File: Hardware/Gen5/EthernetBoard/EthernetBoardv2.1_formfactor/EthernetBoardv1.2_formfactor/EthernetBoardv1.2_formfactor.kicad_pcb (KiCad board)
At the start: 4 copper layers, 50 x 40 mm, 78 parts, among them J1 RJ45_Wuerth_7499010211A, J2 Conn_01x19_Pin, J3 Conn_01x19_Pin, J4 Conn_02x07_Odd_Even, J5 USB_C_Receptacle_USB2.0_16P, J6 Conn_01x02_Pin, J7 Conn_01x02_Pin, J9 Conn_01x02_Pin, Q1 SS8050, Q2 SS8050, SW1 SW_Push, SW2 SW_Push, U1 LAN8720A, U3 AMS1117-3.3, U4 CP2102N-Axx-xQFN28, U5 ESP32-WROVER-E-N8R8, Y1 ASCO

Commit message: updates
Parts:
- C14, C15, R13, R35: moved to B.Cu
- moved J2 94.4 mm to (241.2, 70.6)
- moved J3 90.7 mm to (241.2, 106.0)
- moved R13 47.2 mm to (206.7, 92.2), turned to 90 degrees
- moved R35 43.2 mm to (205.2, 96.0)
- moved R33 41.9 mm to (205.6, 96.1)
- moved R34 41.8 mm to (203.6, 95.9)
- moved Q1 41.4 mm to (208.7, 79.4)
- moved R17 40.7 mm to (213.0, 91.0)
- moved U4 40.5 mm to (206.2, 90.9)
- moved Q2 40.1 mm to (204.4, 85.6)
- moved C14 39.9 mm to (203.7, 92.2)
- moved C15 39.9 mm to (205.0, 92.2)
- moved SW2 39.8 mm to (212.8, 80.5), turned to -90 degrees
- moved D5 39.3 mm to (201.6, 95.7)
- moved R16 39.3 mm to (213.0, 88.3)
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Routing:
- net /EN: track 131.3 -> 77.5 mm, vias 1 -> 0
- net VBUS: track 44.9 -> 16.2 mm
- net /TXDUSB: track 58.6 -> 33.5 mm, vias 2 -> 1
- net /RXDUSB: track 54.0 -> 32.3 mm, vias 2 -> 1
- net /IO0: track 157.8 -> 137.7 mm, vias 3 -> 2
- net /TXD: track 19.3 -> 0.00 mm
- net GND: track 64.6 -> 46.4 mm, vias 31 -> 22
- net /DTR: track 16.5 -> 0.00 mm
- net /USB_DN: track 17.5 -> 1.70 mm
- net /RTS: track 13.8 -> 0.00 mm, vias 2 -> 0
- net /RXD: track 10.1 -> 0.00 mm
- net Net-(U4-VBUS): track 7.75 -> 0.00 mm
- net /USB_DP: track 9.20 -> 1.70 mm
- net Net-(U4-~{SUSPEND}): track 5.91 -> 0.00 mm
- net Net-(Q1-B): track 5.31 -> 0.00 mm
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
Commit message: update
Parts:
- removed J2, J3: Conn_01x19_Pin, Connector_PinHeader_2.54mm:PinHeader_1x19_P2.54mm_Vertical
- removed J4: Conn_02x07_Odd_Even, Connector_PinHeader_2.54mm:PinHeader_2x07_P2.54mm_Vertical
- removed J6, J7, J9: Conn_01x02_Pin, Connector_PinHeader_2.54mm:PinHeader_1x02_P2.54mm_Vertical
- removed TP1, TP2: TestPoint, TestPoint:TestPoint_Pad_2.0x2.0mm
- added R36: 10K, Resistor_SMD:R_0402_1005Metric, B.Cu at (208.3, 89.1)
- added R37: 0R, Resistor_SMD:R_0201_0603Metric, B.Cu at (191.4, 99.3)
- added R38: 0R, Resistor_SMD:R_0201_0603Metric, B.Cu at (198.0, 87.4)
- added R39: 0R, Resistor_SMD:R_0201_0603Metric, B.Cu at (177.8, 93.3)
- C1, C10, C11, C12, C13, C2, C5, C6, C7, C8, C9, D1, D2, D3, D5, D7, D8, L1, Q1, Q2, R1, R10, R11, R14, R15, R18, R19, R2, R20, R21, R22, R23, R3, R34, R4, R5, R6, R7, R8, R9, SW1, SW2, U1, U3, Y1: moved to B.Cu
- R12: footprint Jumper:SolderJumper-2_P1.3mm_Bridged2Bar_RoundedPad1.0x1.5mm -> Resistor_SMD:R_0201_0603Metric
- R16, R17, R24, R25, R26, R27, R28, R29, R30, R31, R32: footprint Jumper:SolderJumper-2_P1.3mm_Bridged2Bar_RoundedPad1.0x1.5mm -> Resistor_SMD:R_0201_0603Metric; moved to B.Cu
- moved R27 142.5 mm to (209.0, 100.8), turned to 90 degrees
- moved R28 138.0 mm to (205.2, 100.8), turned to 90 degrees
- moved R31 128.6 mm to (210.3, 100.8), turned to 90 degrees
- moved R30 123.2 mm to (201.4, 100.8), turned to 90 degrees
- moved R32 121.1 mm to (195.0, 103.1), turned to 90 degrees
- moved L1 120.5 mm to (191.8, 97.2), turned to -90 degrees
- moved R12 120.3 mm to (186.1, 97.2), turned to 0 degrees
- moved C8 117.5 mm to (194.5, 98.7)
- moved C4 117.4 mm to (207.1, 107.8), turned to -90 degrees
- moved R10 117.1 mm to (191.3, 92.6)
- moved R20 116.9 mm to (194.6, 97.3), turned to 180 degrees
- moved C11 116.8 mm to (190.9, 90.0), turned to 90 degrees
- moved C3 116.6 mm to (203.1, 107.4), turned to -90 degrees
- moved R8 116.3 mm to (190.3, 96.4), turned to 90 degrees
- moved U3 116.1 mm to (203.9, 107.7), turned to 0 degrees
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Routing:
- net /IO0: track 137.7 -> 0.00 mm, vias 2 -> 0
- net /TXD0: track 136.6 -> 0.00 mm, vias 1 -> 0
- net /RXD0: track 130.4 -> 0.00 mm, vias 3 -> 0
- net /IO21: track 122.9 -> 0.00 mm
- net VCC: track 117.3 -> 0.00 mm, vias 5 -> 0
- net /IO22: track 113.7 -> 0.00 mm, vias 2 -> 0
- net /IO18: track 88.8 -> 0.00 mm, vias 2 -> 0
- net /RXD1: track 85.4 -> 0.00 mm, vias 2 -> 0
- net /IO23: track 84.0 -> 0.00 mm
- net /EN: track 77.5 -> 0.00 mm
- net /CRS_DV: track 72.8 -> 0.00 mm, vias 2 -> 0
- net VDDA: track 70.0 -> 0.00 mm, vias 1 -> 0
- net +5V: track 63.5 -> 0.00 mm
- net GND: track 46.4 -> 0.00 mm, vias 22 -> 0
- net Net-(J1-Pad11): track 38.6 -> 0.00 mm
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- removed copper zone on B.Cu, net Earth
- removed copper zone on F.Cu, net Earth
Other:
- board size 50 x 40 mm -> 48 x 30 mm
- board text removed: "BOOT"
- board text removed: "EN"
- board text removed: "ESP32"
- board text removed: "Ethernet"
- board text removed: "Power"
- board text removed: "USB"

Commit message: updates
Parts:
- C7: footprint Capacitor_SMD:C_0603_1608Metric -> Capacitor_SMD:C_0402_1005Metric
- D8, R18, R39: moved to F.Cu
- moved D8 39.9 mm to (206.3, 109.6)
- moved R18 39.7 mm to (206.3, 106.5)
- moved D2 29.5 mm to (198.9, 108.1)
- moved R39 8.38 mm to (186.1, 92.0), turned to 0 degrees
- moved C1 7.12 mm to (193.8, 103.2), turned to 0 degrees
- moved SW1 2.85 mm to (193.8, 107.5), turned to -90 degrees
- moved U3 2.64 mm to (206.5, 108.2)
- moved C4 2.63 mm to (209.7, 108.2)
- moved R32 1.00 mm to (196.0, 103.1)
- moved C7 0.59 mm to (198.9, 95.0)
- moved C3 0.38 mm to (203.3, 107.1)
- moved R8 0.33 mm to (190.3, 96.7)
- moved R9 0.33 mm to (190.3, 94.7)
- moved R10 0.28 mm to (191.3, 92.3)
- moved D6 0.23 mm to (175.6, 105.9)
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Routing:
- net /EN: track 0.00 -> 54.1 mm, vias 0 -> 1
- net VBUS: track 0.00 -> 46.8 mm, vias 0 -> 1
- net GND: track 0.00 -> 39.5 mm, vias 0 -> 20
- net Net-(J1-Pad11): track 0.00 -> 37.8 mm
- net /RXD: track 0.00 -> 30.9 mm, vias 0 -> 1
- net /TXD: track 0.00 -> 30.3 mm, vias 0 -> 1
- net VDDA: track 0.00 -> 28.9 mm, vias 0 -> 1
- net /TD_N: track 0.00 -> 28.7 mm, vias 0 -> 1
- net /TD_P: track 0.00 -> 27.8 mm, vias 0 -> 1
- net Net-(J1-Pad10): track 0.00 -> 26.0 mm
- net Net-(J1-Pad8): track 0.00 -> 25.5 mm
- net +3.3V: track 0.00 -> 24.2 mm, vias 0 -> 15
- net /TXD1: track 0.00 -> 21.7 mm, vias 0 -> 2
- net /CRS_DV: track 0.00 -> 20.4 mm, vias 0 -> 2
- net /MDC: track 0.00 -> 18.4 mm, vias 0 -> 2
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- added copper zone on In2.Cu, net +3.3V
- added copper zone on B.Cu, net GND
- added copper zone on F.Cu, net GND
- added copper zone on In1.Cu, net GND

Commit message: done
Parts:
- moved C8 2.16 mm to (193.1, 100.3), turned to -90 degrees
- moved R22 2.11 mm to (195.1, 99.3), turned to 180 degrees
- moved R37 1.89 mm to (191.8, 101.1), turned to -90 degrees
- moved R20 0.60 mm to (195.1, 97.6), turned to -90 degrees
- moved R19 0.30 mm to (199.4, 100.1)
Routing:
- net VDDA: track 28.9 -> 62.8 mm, vias 1 -> 0
- net VCC: track 12.9 -> 34.2 mm, vias 2 -> 6
- net /TX_EN: track 0.00 -> 18.8 mm, vias 0 -> 2
- net /TXD0: track 1.69 -> 18.8 mm, vias 1 -> 2
- net GND: track 39.5 -> 53.1 mm, vias 20 -> 26
- net /CLK50: track 12.8 -> 20.6 mm
- net +3.3V: track 24.2 -> 27.8 mm
- net /REFCLKO: track 6.39 -> 3.53 mm
- net Net-(U4-VBUS): track 1.81 -> 4.31 mm, vias 0 -> 1
- net /nRST: track 2.99 -> 5.00 mm
- net +5V: track 7.53 -> 9.36 mm
- net /R_RX_CLK: track 3.34 -> 4.87 mm
- net /RXD: track 30.9 -> 31.7 mm

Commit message: stuff
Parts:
- added R40: 5.1k, Resistor_SMD:R_0603_1608Metric, B.Cu at (169.0, 108.1)
- added R41: 5.1k, Resistor_SMD:R_0603_1608Metric, B.Cu at (169.0, 106.3)
- added R42: 10K, Resistor_SMD:R_0402_1005Metric, F.Cu at (194.2, 105.5)
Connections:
- J5 pad A5: unconnected-(J5-CC1-PadA5) -> Net-(J5-CC1)
- J5 pad B5: unconnected-(J5-CC2-PadB5) -> Net-(J5-CC2)
- R19 pad 1: Net-(U1-MDIO) -> /MDIO
- U1 pad 12: Net-(U1-MDIO) -> /MDIO
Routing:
- net Net-(J5-CC1): track 0.00 -> 20.1 mm, vias 0 -> 1
- net /MDIO: track 0.00 -> 8.16 mm
- net Net-(U1-MDIO): track 5.38 -> 0.00 mm
- net Net-(J5-CC2): track 0.00 -> 4.18 mm
- net GND: track 53.1 -> 55.5 mm, vias 26 -> 28
- net /IO0: track 16.2 -> 17.4 mm
- net +3.3V: track 27.8 -> 28.8 mm, vias 15 -> 16

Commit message: stuff
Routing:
- net /IO0: vias 2 -> 1
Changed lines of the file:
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@@
 		(tags "resistor")
 		(property "Reference" "R22"
-			(at 0.1 0.9 0)
+			(at -0.91 1.3 90)
 			(layer "B.SilkS")
 			(effects
@@
 		(tags "capacitor")
 		(property "Reference" "C7"
-			(at 0 1.16 90)
+			(at 1.42 0 180)
 			(layer "B.SilkS")
 			(effects
 				(font
-					(size 1 1)
-					(thickness 0.15)
+					(size 0.5 0.5)
+					(thickness 0.125)
+					(bold yes)
 				)
 				(justify mirror)
@@
 		(tags "inductor")
 		(property "Reference" "L1"
-			(at 0.1 1.2 90)
+			(at 1.925 0.1 180)
 			(layer "B.SilkS")
 			(effects
@@
 		(tags "resistor")
 		(property "Reference" "R13"
-			(at 2 0 0)
+			(at 0.275 1.2 90)
 			(layer "B.SilkS")
 			(effects
@@
 		(tags "SOT TO_SOT_SMD")
 		(property "Reference" "Q1"
-			(at -1.3375 2.55 90)
+			(at -2.4375 0.95 180)
 			(layer "B.SilkS")
 			(effects
@@
 		(tags "resistor")
 		(property "Reference" "R7"
-			(at -1.49 0 0)
+			(at 0.025 0.9 90)
 			(layer "B.SilkS")
 			(effects
@@
 		(tags "resistor")
 		(property "Reference" "R20"
-			(at -1.81 0 90)
+			(at 0 0.9 90)
 			(layer "B.SilkS")
 			(effects
@@
 		(net 21)
 	)
-	(via
-		(at 194.8 104.4)
-		(size 0.6)
-		(drill 0.3)
-		(layers "F.Cu" "B.Cu")
-		(net 21)
-	)

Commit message: stuff
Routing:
- net GND: track 55.5 -> 54.8 mm, vias 28 -> 29
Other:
- board text added: "Ethernet Form Factor Gen 5 rev1.2"
- board text removed: "Ethernet Dev Board - Vine Internal rev 1.1 Charm Lab, Stanford October 19 2025"
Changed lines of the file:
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@@
 		(layer "Edge.Cuts")
 	)
-	(gr_text "Ethernet Dev Board - Vine Internal rev 1.1\nCharm Lab, Stanford\nOctober 19 2025"
-		(at 224 124.1 0)
-		(layer "B.SilkS")
+	(gr_text "Ethernet Form Factor\nGen 5\nrev1.2"
+		(at 185.2 111.6 0)
+		(layer "F.SilkS")
 		(effects
 			(font
-				(size 1 1)
-				(thickness 0.25)
+				(size 0.8 0.8)
+				(thickness 0.2)
 				(bold yes)
 			)
-			(justify left bottom mirror)
+			(justify left bottom)
 		)
 	)
@@
 	)
 	(segment
-		(start 211.525 85.611638)
-		(end 211.525 84.675)
-		(width 0.2)
-		(layer "F.Cu")
-		(net 4)
-	)
-	(segment
 		(start 211.525 101.875)
 		(end 211.7 101.7)
@@
 	)
 	(segment
-		(start 211.525 84.675)
-		(end 211.7 84.5)
-		(width 0.2)
-		(layer "F.Cu")
-		(net 4)
-	)
-	(segment
 		(start 186.42 96.68)
 		(end 186.6 96.5)
@@
 	)
 	(segment
+		(start 211.525 84.675)
+		(end 211.525 85.611638)
+		(width 0.2)
+		(layer "F.Cu")
+		(net 4)
+	)
+	(segment
 		(start 179.8 106.925)
 		(end 179.8 106.9)
@@
 	)
 	(segment
+		(start 211.5 84.65)
+		(end 211.525 84.675)
+		(width 0.2)
+		(layer "F.Cu")
+		(net 4)
+	)
+	(segment
+		(start 211.5 84.4)
+		(end 211.5 84.65)
+		(width 0.2)
+		(layer "F.Cu")
+		(net 4)
+	)
+	(segment
 		(start 176.474528 106.3866)
 		(end 177.3116 106.3866)
@@
 	)
 	(via
-		(at 211.7 84.5)
+		(at 211.5 84.4)
 		(size 0.6)
 		(drill 0.3)
@@
 	)
 	(via
+		(at 207.9 97.1)
+		(size 0.6)
+		(drill 0.3)
+		(layers "F.Cu" "B.Cu")
+		(net 4)
+	)
+	(via
 		(at 199.6 95.5)
 		(size 0.6)
@@
 	)
 	(segment
+		(start 207.925 97.075)
+		(end 207.9 97.1)
+		(width 0.2)
+		(layer "B.Cu")
+		(net 4)
+	)
+	(segment
 		(start 173.65 104.325)
 		(end 172.3 104.325)
@@
 	)
 	(segment
-		(start 211.7 84.5)
-		(end 211.7 85.075)
-		(width 0.2)
-		(layer "B.Cu")
-		(net 4)
-	)
-	(segment
 		(start 207.6 95.4)
 		(end 207.7 95.4)
@@
 	)
 	(segment
-		(start 208.925 95.75)
-		(end 208.625 95.45)
-		(width 0.2)
-		(layer "B.Cu")
-		(net 4)
-	)
-	(segment
 		(start 172.3 110.275)
 		(end 171.275 110.275)
@@
 	)
 	(segment
+		(start 208.925 97.075)
+		(end 207.925 97.075)
+		(width 0.2)
+		(layer "B.Cu")
+		(net 4)
+	)
+	(segment
 		(start 173.65 110.275)
 		(end 172.3 110.275)
@@
 	)
 	(segment
-		(start 208.925 97.075)
-		(end 208.925 95.75)
-		(width 0.2)
-		(layer "B.Cu")
-		(net 4)
-	)
-	(segment
 		(start 208.625 91.3)
 		(end 207.5 91.3)
@@
 	)
 	(segment
+		(start 211.5 84.4)
+		(end 211.5 85.275)
+		(width 0.2)
+		(layer "B.Cu")
+		(net 4)
+	)
+	(segment
 		(start 192.725 105.4)
 		(end 192.725 104.53664)
@@
 	)
 	(segment
+		(start 211.5 85.275)
+		(end 211.4 85.375)
+		(width 0.2)
+		(layer "B.Cu")
+		(net 4)
+	)
+	(segment
 		(start 178.145 109.095)
 		(end 178.6 109.55)
@@
 	)
 	(segment
-		(start 211.7 85.075)
-		(end 211.4 85.375)
-		(width 0.2)
-		(layer "B.Cu")
-		(net 4)
-	)
-	(segment
 		(start 175.625 109.3)
 		(end 175.625 110.375)
@@
 	)
 	(segment
-		(start 199.5 90.8)
-		(end 199.699 90.601)
+		(start 199.699 86.449)
+		(end 198.8 85.55)
 		(width 0.2)
 		(layer "B.Cu")
@@
 	)
 	(segment
-		(start 199.699 90.601)
-		(end 199.699 85.794)
+		(start 200.225 93.175)
+		(end 199.4 92.35)
 		(width 0.2)
 		(layer "B.Cu")
@@
 	)
 	(segment
-		(start 200.225 93.175)
-		(end 199.5 92.45)
+		(start 199.4 90.9)
+		(end 199.699 90.601)
 		(width 0.2)
 		(layer "B.Cu")
@@
 	)
 	(segment
-		(start 199.699 85.794)
+		(start 198.8 85.55)
 		(end 198.8 84.895)
 		(width 0.2)
@@
 	)
 	(segment
-		(start 199.5 92.45)
-		(end 199.5 90.8)
+		(start 199.4 92.35)
+		(end 199.4 90.9)
+		(width 0.2)
+		(layer "B.Cu")
+		(net 98)
+	)
+	(segment
+		(start 199.699 90.601)
+		(end 199.699 86.449)
 		(width 0.2)
 		(layer "B.Cu")
@@
 	)
 	(segment
-		(start 204 96.875)
-		(end 205.125 96.875)
+		(start 199.099 86.906147)
+		(end 199.099 86.899)
 		(width 0.2)
 		(layer "B.Cu")
@@
 	)
 	(segment
-		(start 197.5 84.895)
-		(end 197.5 85.307147)
+		(start 197.5 85.3)
+		(end 197.5 84.895)
+		(width 0.2)
+		(layer "B.Cu")
+		(net 99)
+	)
+	(segment
+		(start 204 96.875)
+		(end 205.125 96.875)
 		(width 0.2)
 		(layer "B.Cu")
@@
 	)
 	(segment
-		(start 206.2 88.5)
-		(end 205 87.3)
+		(start 199.099 86.899)
+		(end 197.5 85.3)
 		(width 0.2)
 		(layer "B.Cu")
@@
 	)
 	(segment
-		(start 197.5 85.307147)
-		(end 199.099 86.906147)
+		(start 206.2 88.5)
+		(end 205 87.3)
 		(width 0.2)
 		(layer "B.Cu")

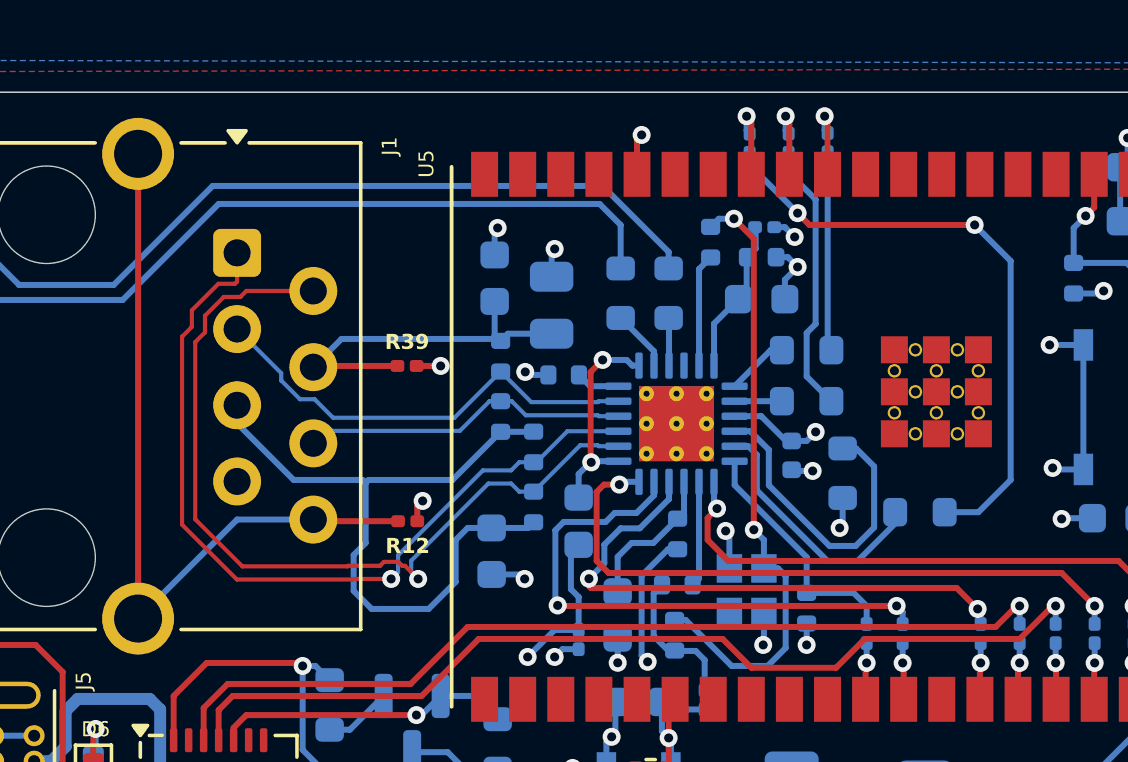
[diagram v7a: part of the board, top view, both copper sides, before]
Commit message: Updated length Matching
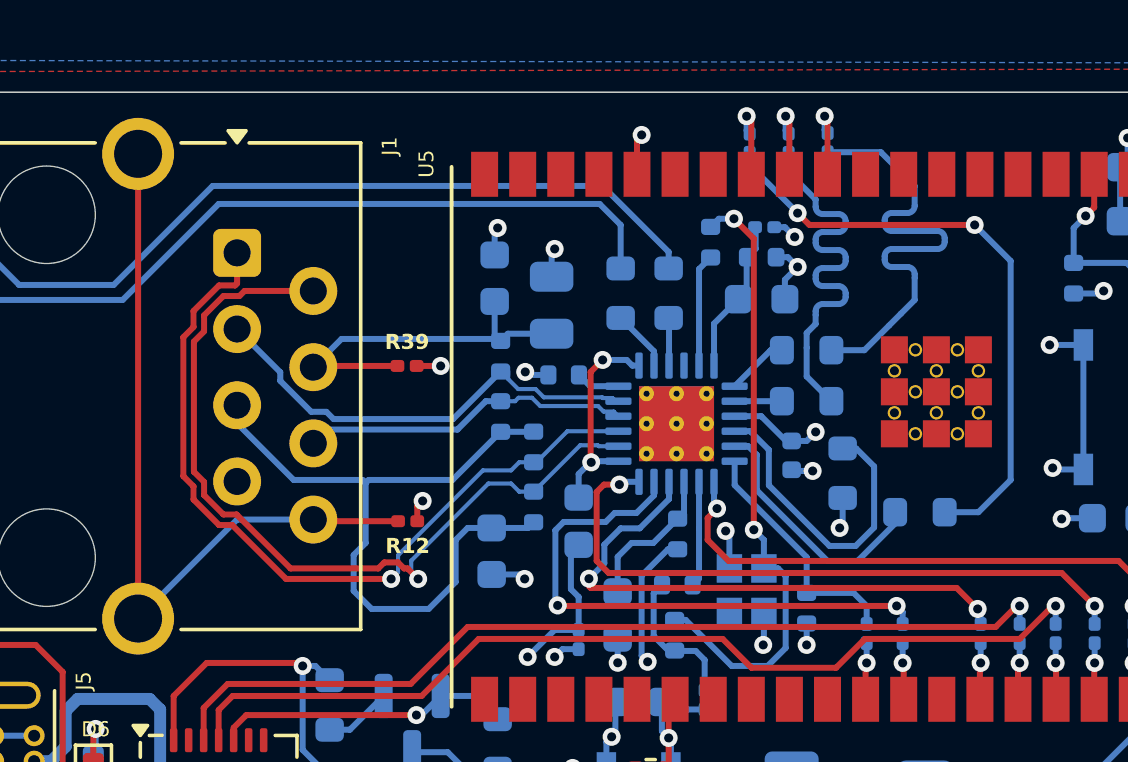
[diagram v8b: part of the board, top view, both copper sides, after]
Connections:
- U5 pad 39_2: GND -> (no net)
- U5 pad 39_3: GND -> (no net)
- U5 pad 39_4: GND -> (no net)
- U5 pad 39_5: GND -> (no net)
- U5 pad 39_6: GND -> (no net)
- U5 pad 39_7: GND -> (no net)
- U5 pad 39_8: GND -> (no net)
- U5 pad 39_9: GND -> (no net)
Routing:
- net /RXD0: track 6.65 -> 15.7 mm
- net /RXD1: track 9.12 -> 13.8 mm
- net /TD_P: track 27.8 -> 27.0 mm
- net /TD_N: track 28.7 -> 28.2 mm
